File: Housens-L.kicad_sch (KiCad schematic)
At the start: 36 parts, among them J1 JTAG/SWD, SW1 RESET, U1 MCP1603, U2 BME280, U3 OPT3005, U4 STM32WB55CGUx, Y1 32MHz, Y2 32.768kHz

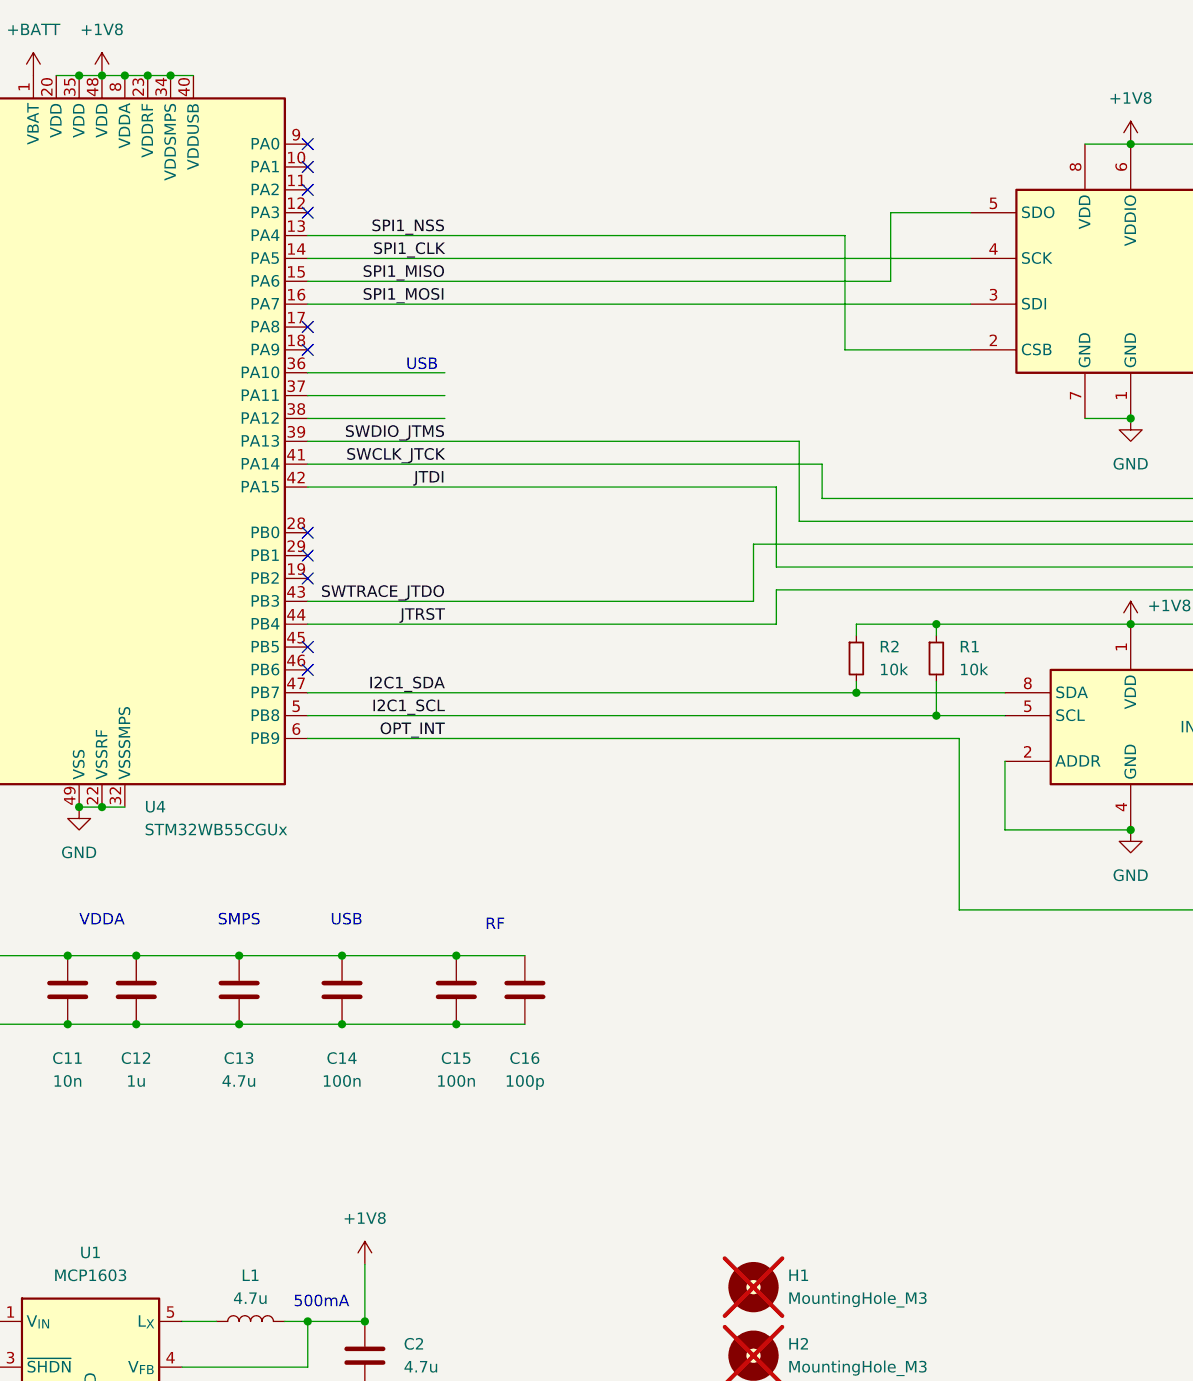
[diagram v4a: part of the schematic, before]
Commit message: Add USB connector
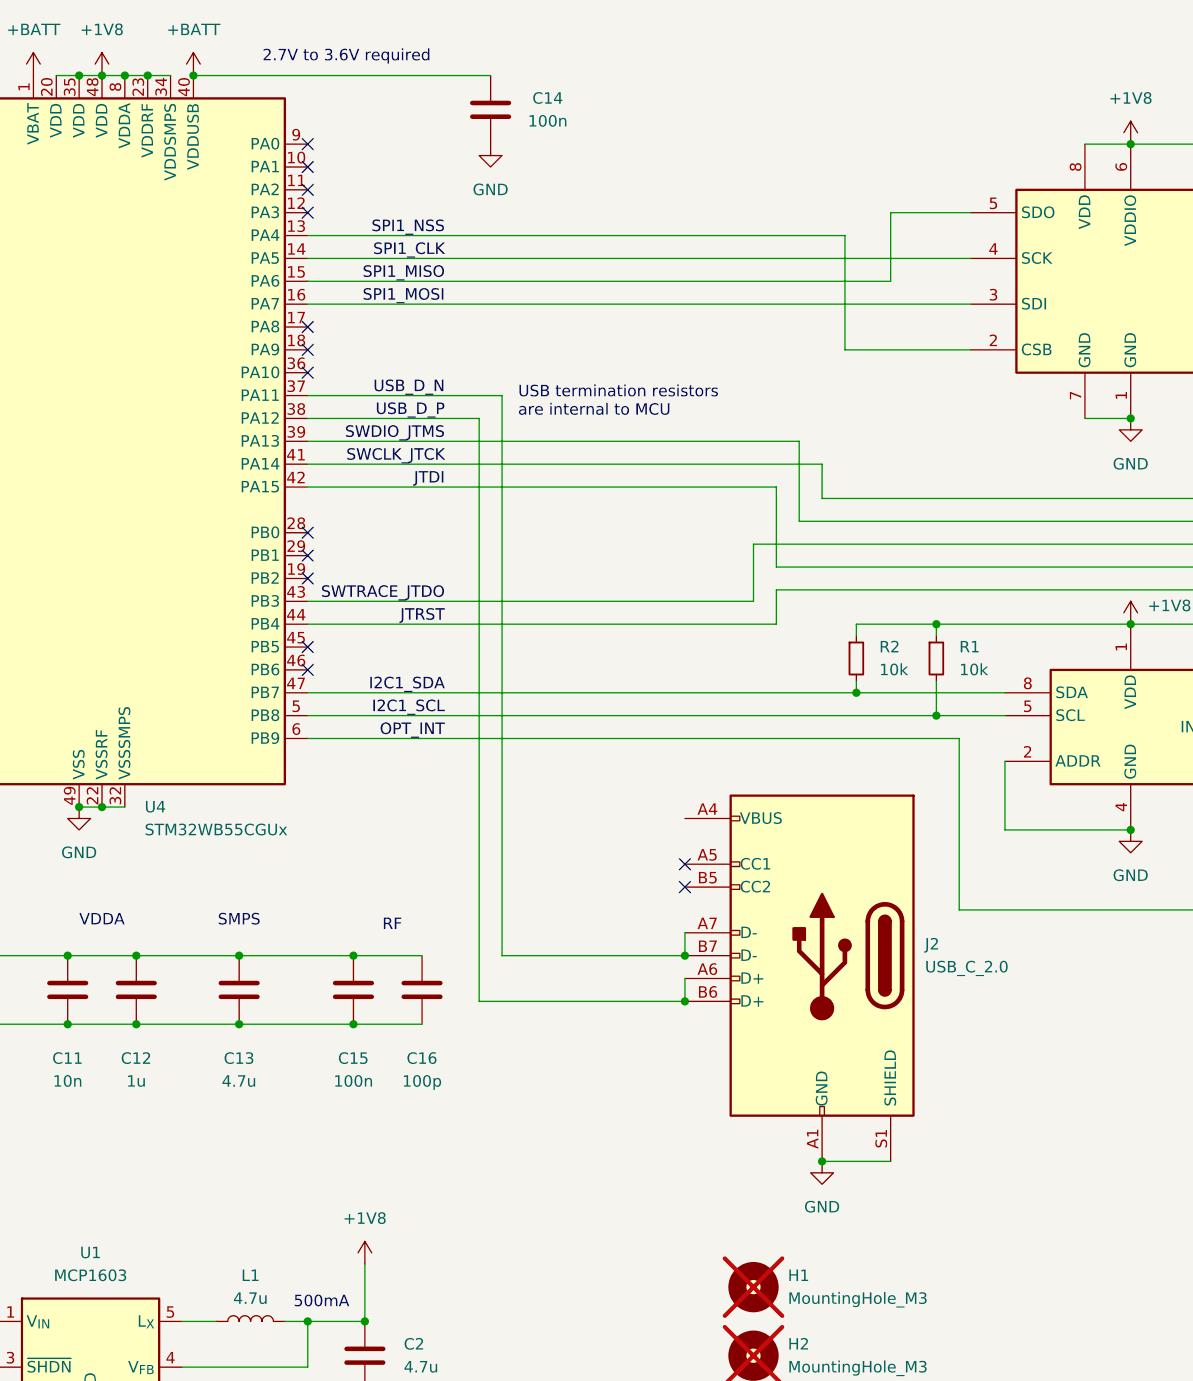
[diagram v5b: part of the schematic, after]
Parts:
- added J2: USB_C_2.0, Connector_USB:USB_C_Receptacle_G-Switch_GT-USB-7010ASV, symbol Connector:USB_C_Receptacle_USB2.0_14P
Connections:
- net +1V8: no longer C14.1, U4.40 (VDDUSB)
- net +BATT: now also C14.1, U4.40 (VDDUSB)
- net GND: now also J2.A1 (GND), J2.A12 (GND), J2.B1 (GND), J2.B12 (GND), J2.S1 (SHIELD)
- net USB_D_N: now reaches U4.37 (PA11)
- net USB_D_N: now also J2.A7 (D-), J2.B7 (D-)
- net USB_D_P: now reaches U4.38 (PA12)
- net USB_D_P: now also J2.A6 (D+), J2.B6 (D+)
- new net: J2.A4 (VBUS), J2.A9 (VBUS), J2.B4 (VBUS), J2.B9 (VBUS)
- no-connect marks 11 -> 14
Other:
- note added: "2.7V to 3.6V required"
- note added: "USB termination resistors are internal to MCU"
- note removed: "USB"
- moved on the sheet: C14, C15, C16

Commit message: Initial spatial layout
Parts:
- AE1: footprint (none) -> RF_Antenna:Texas_SWRA117D_2.4GHz_Right
- U3: footprint OPT3005DTSR -> Imported:OPT3005DTSR
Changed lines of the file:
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@@
 			)
 		)
-		(property "Footprint" "OPT3005DTSR"
+		(property "Footprint" "Imported:OPT3005DTSR"
 			(at 180.34 195.25 0)
 			(effects
@@
 			)
 		)
-		(property "Footprint" ""
+		(property "Footprint" "RF_Antenna:Texas_SWRA117D_2.4GHz_Right"
 			(at 33.02 57.15 0)
 			(effects

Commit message: Graphics
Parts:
- removed H2, H3: MountingHole_M3, MountingHole:MountingHole_3.2mm_M3, symbol PCM_SL_Mechanical:MountingHole_M3
- added H2, H3: MountingHole_Pad, MountingHole:MountingHole_3.2mm_M3_DIN965_Pad, symbol Mechanical:MountingHole_Pad
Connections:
- net GND: now also H2.1
- net CELL: now reaches BT1.1 (+), D1.2 (A)
- net CELL: now also H3.1
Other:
- note added: "mounting holes"
- moved on the sheet: D1, H1, H4

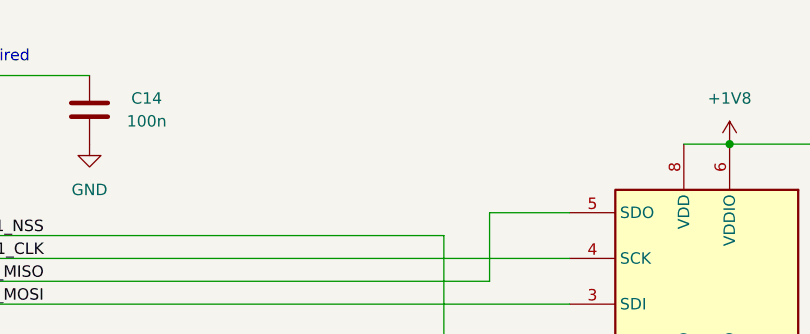
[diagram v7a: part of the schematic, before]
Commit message: Add TODO about touchsense
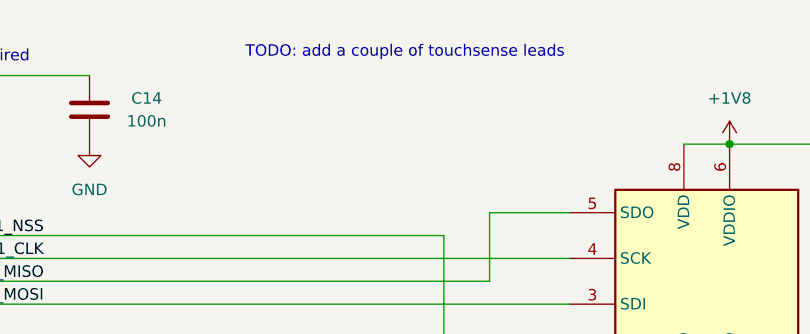
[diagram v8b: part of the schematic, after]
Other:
- note added: "TODO: add a couple of touchsense leads"
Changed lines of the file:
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@@
+		)
+	)
+	(text "TODO: add a couple of touchsense leads"
+		(exclude_from_sim no)
+		(at 154.432 29.21 0)
+		(effects
+			(font
+				(size 1.27 1.27)
+			)
 		)
 	)
